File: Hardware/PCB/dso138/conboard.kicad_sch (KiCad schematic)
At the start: 33 parts, among them J1 Synth_power_2x5, SW1 SW_Push, SW2 SW_Push, SW3 SW_Push, SW4 SW_Push, SW5 SW_Push, SW6 SW_DP3T, SW7 SW_DP3T, SW8 SW_DP3T, U1 TL072, U2 L78L09_TO92

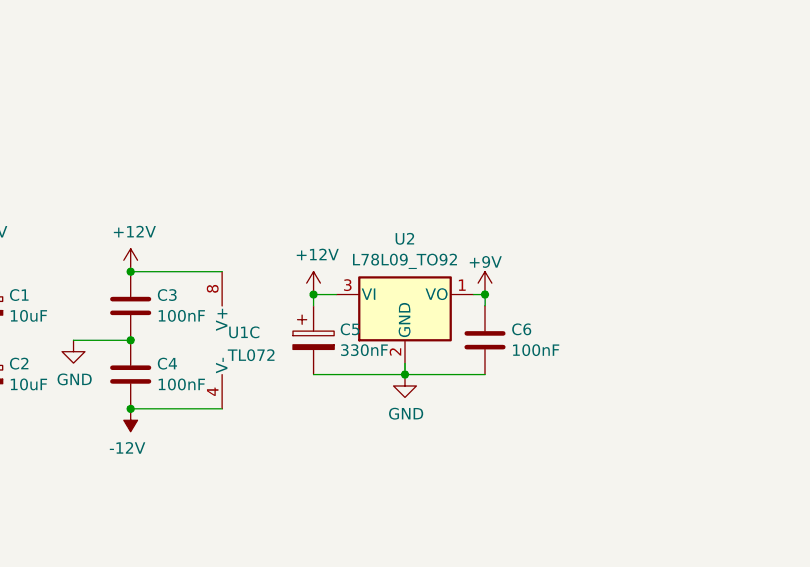
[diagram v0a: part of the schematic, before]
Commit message: TO-220 regulator; panel
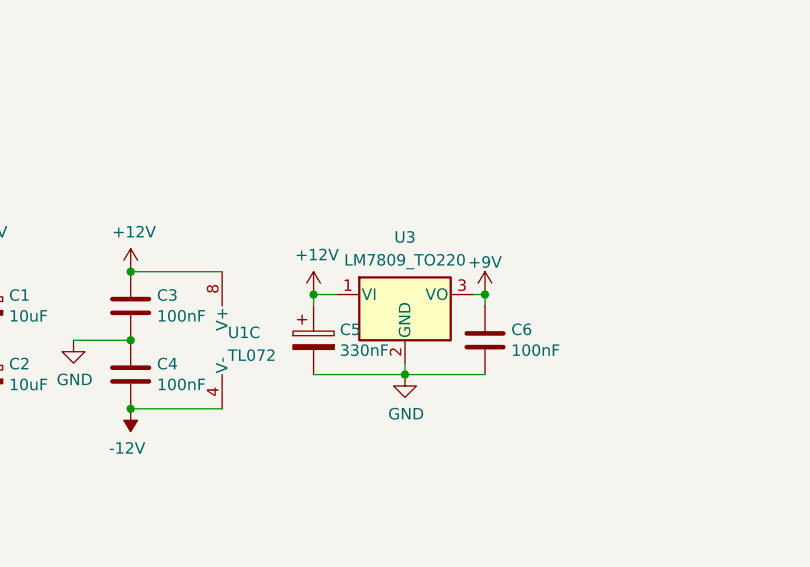
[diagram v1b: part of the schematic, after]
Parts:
- removed U2: L78L09_TO92, AO_tht:TO-92_Inline_Wide, symbol AO_symbols:L78L09_TO92
- added U3: LM7809_TO220, Package_TO_SOT_THT:TO-220-3_Vertical, symbol Regulator_Linear:LM7809_TO220
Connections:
- net +12V: now also U3.1 (VI)
- net +9V: now also U3.3 (VO)
- net GND: now also U3.2 (GND)
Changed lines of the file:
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@@
-    )
-  )
-  (symbol (lib_id "AO_symbols:L78L09_TO92") (at 153.67 149.86 0) (unit 1)
-    (in_bom yes) (on_board yes) (dnp no)
-    (property "Reference" "U2" (at 153.67 143.7132 0)
-      (effects (font (size 1.27 1.27)))
-    )
-    (property "Value" "L78L09_TO92" (at 153.67 146.0246 0)
-      (effects (font (size 1.27 1.27)))
-    )
-    (property "Footprint" "AO_tht:TO-92_Inline_Wide" (at 153.67 144.145 0)
-      (effects (font (size 1.27 1.27) italic) hide)
-    )
-    (property "Datasheet" "http://www.st.com/content/ccc/resource/technical/document/datasheet/15/55/e5/aa/23/5b/43/fd/CD00000446.pdf/files/CD00000446.pdf/jcr:content/translations/en.CD00000446.pdf" (at 153.67 151.13 0)
-      (effects (font (size 1.27 1.27)) hide)
-    )
-    (property "Vendor" "Tayda" (at 153.67 149.86 0)
-      (effects (font (size 1.27 1.27)) hide)
-    )
-    (property "SKU" "A-878" (at 153.67 149.86 0)
-      (effects (font (size 1.27 1.27)) hide)
-    )
-    (pin "1")
-    (pin "2")
-    (pin "3")
-    (instances
-      (project "dso138"
-        (path "/1fce46f5-2003-4c7e-915f-b9b7dfc679d7"
-          (reference "U2") (unit 1)
-        )
-        (path "/1fce46f5-2003-4c7e-915f-b9b7dfc679d7/19824610-a3fe-48b6-8f41-5007805ab8a3"
-          (reference "U2") (unit 1)
-        )
-      )
     )
   )
@@
         )
       )
+    )
+  )
+  (symbol (lib_id "Regulator_Linear:LM7809_TO220") (at 153.67 149.86 0) (unit 1)
+    (in_bom yes) (on_board yes) (dnp no) (fields_autoplaced)
+    (property "Reference" "U3" (at 153.67 143.51 0)
+      (effects (font (size 1.27 1.27)))
+    )
+    (property "Value" "LM7809_TO220" (at 153.67 146.05 0)
+      (effects (font (size 1.27 1.27)))
+    )
+    (property "Footprint" "Package_TO_SOT_THT:TO-220-3_Vertical" (at 153.67 144.145 0)
+      (effects (font (size 1.27 1.27) italic) hide)
+    )
+    (property "Datasheet" "https://www.onsemi.cn/PowerSolutions/document/MC7800-D.PDF" (at 153.67 151.13 0)
+      (effects (font (size 1.27 1.27)) hide)
+    )
+    (pin "1")
+    (pin "2")
+    (pin "3")
+    (instances
+      (project "dso138"
+        (path "/1fce46f5-2003-4c7e-915f-b9b7dfc679d7/19824610-a3fe-48b6-8f41-5007805ab8a3"
+          (reference "U3") (unit 1)
+        )
+      )

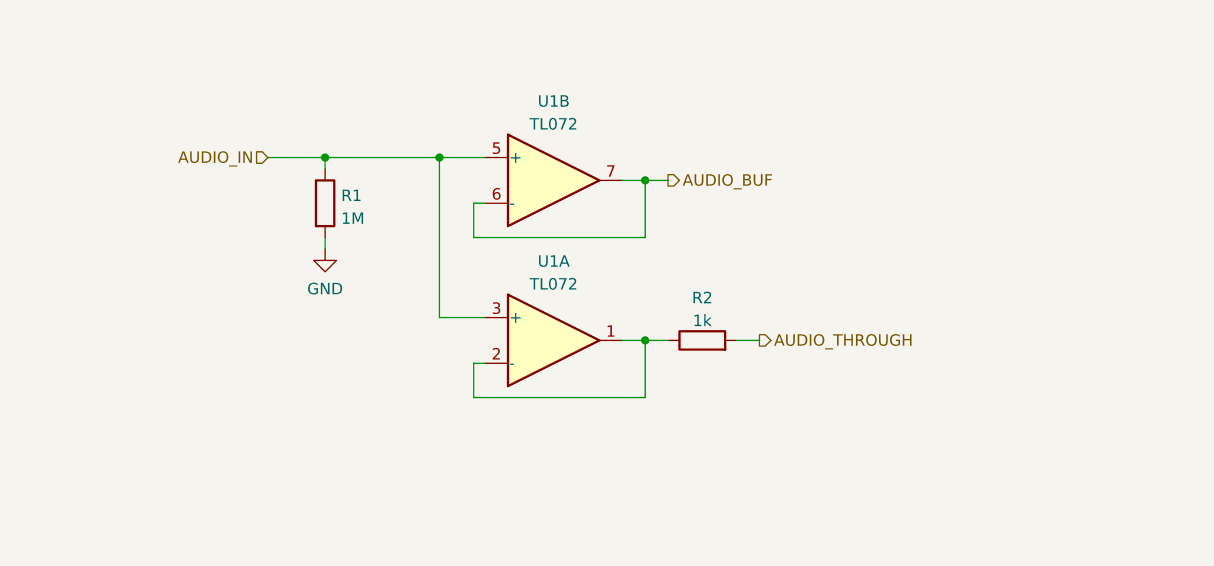
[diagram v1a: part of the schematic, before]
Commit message: Net classes, move 7809 and make horizontal, inverting buffers, power switch via PCB
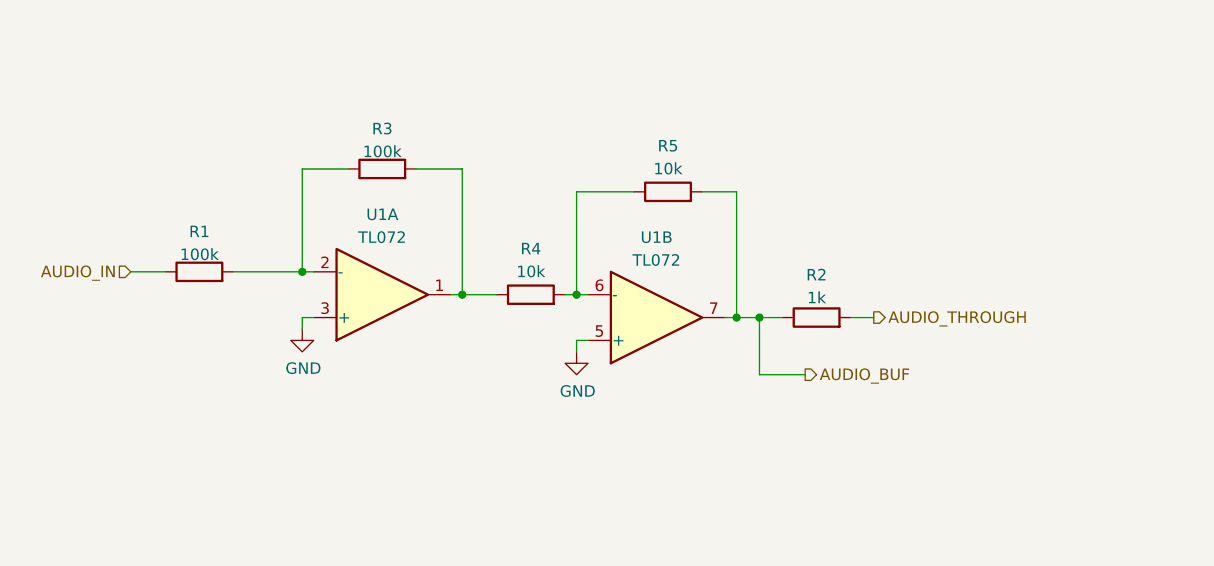
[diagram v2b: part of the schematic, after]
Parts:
- added R3: 100k, AO_tht:R_Axial_DIN0207_L6.3mm_D2.5mm_P10.16mm_Horizontal, symbol AO_symbols:R
- added R4, R5: 10k, AO_tht:R_Axial_DIN0207_L6.3mm_D2.5mm_P10.16mm_Horizontal, symbol AO_symbols:R
- R1: value 1M -> 100k
- U3: footprint Package_TO_SOT_THT:TO-220-3_Vertical -> Package_TO_SOT_THT:TO-220-3_Horizontal_TabDown
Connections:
- net AUDIO_BUF: now also R2.1, R5.2; no longer U1.6 (-)
- net AUDIO_IN: no longer U1.3 (+), U1.5 (+)
- net GND: now also U1.3 (+), U1.5 (+); no longer R1.2
- new net: R4.2, R5.1, U1.6 (-)
- new net: R3.2, R4.1, U1.1
- new net: R1.2, R3.1, U1.2 (-)
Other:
- moved on the sheet: R2

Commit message: Mechanicals
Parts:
- removed GRAF1: Behind, dso138:dso138_behind, symbol AO_symbols:Graphic
- GRAF2, GRAF3, H1, H2, H3, H4, TP1, TP2, TP3, TP4: Config DNF -> (none)
- renumbered R3 to R2, R4 to R3, R5 to R4, U3 to U2

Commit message: STL file; BOM; documentation
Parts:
- SW1, SW2, SW3, SW4, SW5: Manufacturer (none) -> E-Switch; Part (none) -> TL1100F160Q; SKU A-3487 -> EG1821-ND; Vendor Tayda -> Digi-Key
- U2: SKU (none) -> A-1597; Vendor (none) -> Tayda
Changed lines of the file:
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@@
+      (effects (font (size 1.27 1.27)) hide)
+    )
+    (property "Description" "2x5 pin shrouded pin header, 2.54 mm pitch" (at 52.07 154.94 0)
       (effects (font (size 1.27 1.27)) hide)
     )
@@
       (effects (font (size 1.27 1.27)) hide)
     )
+    (property "Description" "DP3T slide switch" (at 175.26 72.39 0)
+      (effects (font (size 1.27 1.27)) hide)
+    )
     (pin "1")
     (pin "2")
@@
       (effects (font (size 1.27 1.27)) hide)
     )
-    (property "Vendor" "Tayda" (at 229.87 46.99 0)
-      (effects (font (size 1.27 1.27)) hide)
-    )
-    (property "SKU" "A-3487" (at 229.87 46.99 0)
+    (property "Vendor" "Digi-Key" (at 229.87 46.99 0)
+      (effects (font (size 1.27 1.27)) hide)
+    )
+    (property "SKU" "EG1821-ND" (at 229.87 46.99 0)
+      (effects (font (size 1.27 1.27)) hide)
+    )
+    (property "Description" "Tactile push button" (at 229.87 46.99 0)
+      (effects (font (size 1.27 1.27)) hide)
+    )
+    (property "Manufacturer" "E-Switch" (at 229.87 46.99 0)
+      (effects (font (size 1.27 1.27)) hide)
+    )
+    (property "Part" "TL1100F160Q" (at 229.87 46.99 0)
       (effects (font (size 1.27 1.27)) hide)
     )
@@
       (effects (font (size 1.27 1.27)) hide)
     )
-    (property "Vendor" "Tayda" (at 229.87 64.77 0)
-      (effects (font (size 1.27 1.27)) hide)
-    )
-    (property "SKU" "A-3487" (at 229.87 64.77 0)
+    (property "Vendor" "Digi-Key" (at 229.87 64.77 0)
+      (effects (font (size 1.27 1.27)) hide)
+    )
+    (property "SKU" "EG1821-ND" (at 229.87 64.77 0)
+      (effects (font (size 1.27 1.27)) hide)
+    )
+    (property "Description" "Tactile push button" (at 229.87 64.77 0)
+      (effects (font (size 1.27 1.27)) hide)
+    )
+    (property "Manufacturer" "E-Switch" (at 229.87 64.77 0)
+      (effects (font (size 1.27 1.27)) hide)
+    )
+    (property "Part" "TL1100F160Q" (at 229.87 64.77 0)
       (effects (font (size 1.27 1.27)) hide)
     )
@@
     )
     (property "SKU" "CKN9554-ND" (at 175.26 60.96 0)
+      (effects (font (size 1.27 1.27)) hide)
+    )
+    (property "Description" "DP3T slide switch" (at 175.26 60.96 0)
       (effects (font (size 1.27 1.27)) hide)
     )
@@
       (effects (font (size 1.27 1.27)) hide)
     )
+    (property "Description" "DP3T slide switch" (at 175.26 46.99 0)
+      (effects (font (size 1.27 1.27)) hide)
+    )
     (pin "1")
     (pin "2")
@@
       (effects (font (size 1.27 1.27)) hide)
     )
+    (property "SKU" "A-1597" (at 153.67 149.86 0)
+      (effects (font (size 1.27 1.27)) hide)
+    )
+    (property "Vendor" "Tayda" (at 153.67 149.86 0)
+      (effects (font (size 1.27 1.27)) hide)
+    )
     (pin "1")
     (pin "2")
@@
     )
     (property "SKU" "CKN9554-ND" (at 175.26 35.56 0)
+      (effects (font (size 1.27 1.27)) hide)
+    )
+    (property "Description" "DP3T slide switch" (at 175.26 35.56 0)
       (effects (font (size 1.27 1.27)) hide)
     )
@@
       (effects (font (size 1.27 1.27)) hide)
     )
-    (property "Vendor" "Tayda" (at 229.87 73.66 0)
-      (effects (font (size 1.27 1.27)) hide)
-    )
-    (property "SKU" "A-3487" (at 229.87 73.66 0)
+    (property "Vendor" "Digi-Key" (at 229.87 73.66 0)
+      (effects (font (size 1.27 1.27)) hide)
+    )
+    (property "SKU" "EG1821-ND" (at 229.87 73.66 0)
+      (effects (font (size 1.27 1.27)) hide)
+    )
+    (property "Description" "Tactile push button" (at 229.87 73.66 0)
+      (effects (font (size 1.27 1.27)) hide)
+    )
+    (property "Manufacturer" "E-Switch" (at 229.87 73.66 0)
+      (effects (font (size 1.27 1.27)) hide)
+    )
+    (property "Part" "TL1100F160Q" (at 229.87 73.66 0)
       (effects (font (size 1.27 1.27)) hide)
     )
@@
     )
     (property "SKU" "CKN9554-ND" (at 175.26 97.79 0)
+      (effects (font (size 1.27 1.27)) hide)
+    )
+    (property "Description" "DP3T slide switch" (at 175.26 97.79 0)
       (effects (font (size 1.27 1.27)) hide)
     )
@@
       (effects (font (size 1.27 1.27)) hide)
     )
+    (property "Description" "DP3T slide switch" (at 175.26 86.36 0)
+      (effects (font (size 1.27 1.27)) hide)
+    )
     (pin "1")
     (pin "2")
@@
       (effects (font (size 1.27 1.27)) hide)
     )
-    (property "Vendor" "Tayda" (at 229.87 82.55 0)
-      (effects (font (size 1.27 1.27)) hide)
-    )
-    (property "SKU" "A-3487" (at 229.87 82.55 0)
+    (property "Vendor" "Digi-Key" (at 229.87 82.55 0)
+      (effects (font (size 1.27 1.27)) hide)
+    )
+    (property "SKU" "EG1821-ND" (at 229.87 82.55 0)
+      (effects (font (size 1.27 1.27)) hide)
+    )
+    (property "Description" "Tactile push button" (at 229.87 82.55 0)
+      (effects (font (size 1.27 1.27)) hide)
+    )
+    (property "Manufacturer" "E-Switch" (at 229.87 82.55 0)
+      (effects (font (size 1.27 1.27)) hide)
+    )
+    (property "Part" "TL1100F160Q" (at 229.87 82.55 0)
       (effects (font (size 1.27 1.27)) hide)
     )
@@
       (effects (font (size 1.27 1.27)) hide)
     )
-    (property "Vendor" "Tayda" (at 229.87 55.88 0)
-      (effects (font (size 1.27 1.27)) hide)
-    )
-    (property "SKU" "A-3487" (at 229.87 55.88 0)
-      (effects (font (size 1.27 1.27)) hide)
-    )
+    (property "Vendor" "Digi-Key" (at 229.87 55.88 0)
+      (effects (font (size 1.27 1.27)) hide)
+    )
+    (property "SKU" "EG1821-ND" (at 229.87 55.88 0)
+      (effects (font (size 1.27 1.27)) hide)
+    )
+    (property "Description" "Tactile push button" (at 229.87 55.88 0)
+      (effects (font (size 1.27 1.27)) hide)
+    )
+    (property "Manufacturer" "E-Switch" (at 229.87 55.88 0)
+      (effects (font (size 1.27 1.27)) hide)
+    )
+    (property "Part" "TL1100F160Q" (at 229.87 55.88 0)
+      (effects (font (size 1.27 1.27)) hide)
+    )

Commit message: BOM correction
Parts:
- C6: SKU A-962 -> A-553
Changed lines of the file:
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@@
       (effects (font (size 1.27 1.27)) hide)
     )
-    (property "SKU" "A-962" (at 162.56 154.94 0)
+    (property "SKU" "A-553" (at 162.56 154.94 0)
       (effects (font (size 1.27 1.27)) hide)
     )
